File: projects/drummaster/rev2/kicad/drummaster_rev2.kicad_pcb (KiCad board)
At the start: 2 copper layers, 99.7 x 99.7 mm, 183 parts, among them K1 PINS_5, K1 PINS_7, K1 TSSOP-28, K2 DIP, K2 PINS_5, K2 PINS_7, K3 DIP, K3 MSSOP_10, K3 PINS_5, K4 PINS_4, K4 TSSOP_14, K5 PINS_6, K6 PINS_4, K7 ENCODER, P1 CONN_2, Q1 MOSFET_P, SW1 PROG, U1 TEENSY_3.1, U10 MCP46X1, U11 MCP46X1, U12 MCP46X1, U13 MCP46X1, U14 MCP46X1, U15 MCP46X1, U16 S25FL512S, U2 MCP6004T, U3 MCP6004T, U4 MCP6004T, U5 MCP6004T, U6 MCP6004T, U7 MCP6004T, U8 74HC4067, U9 74HC4067

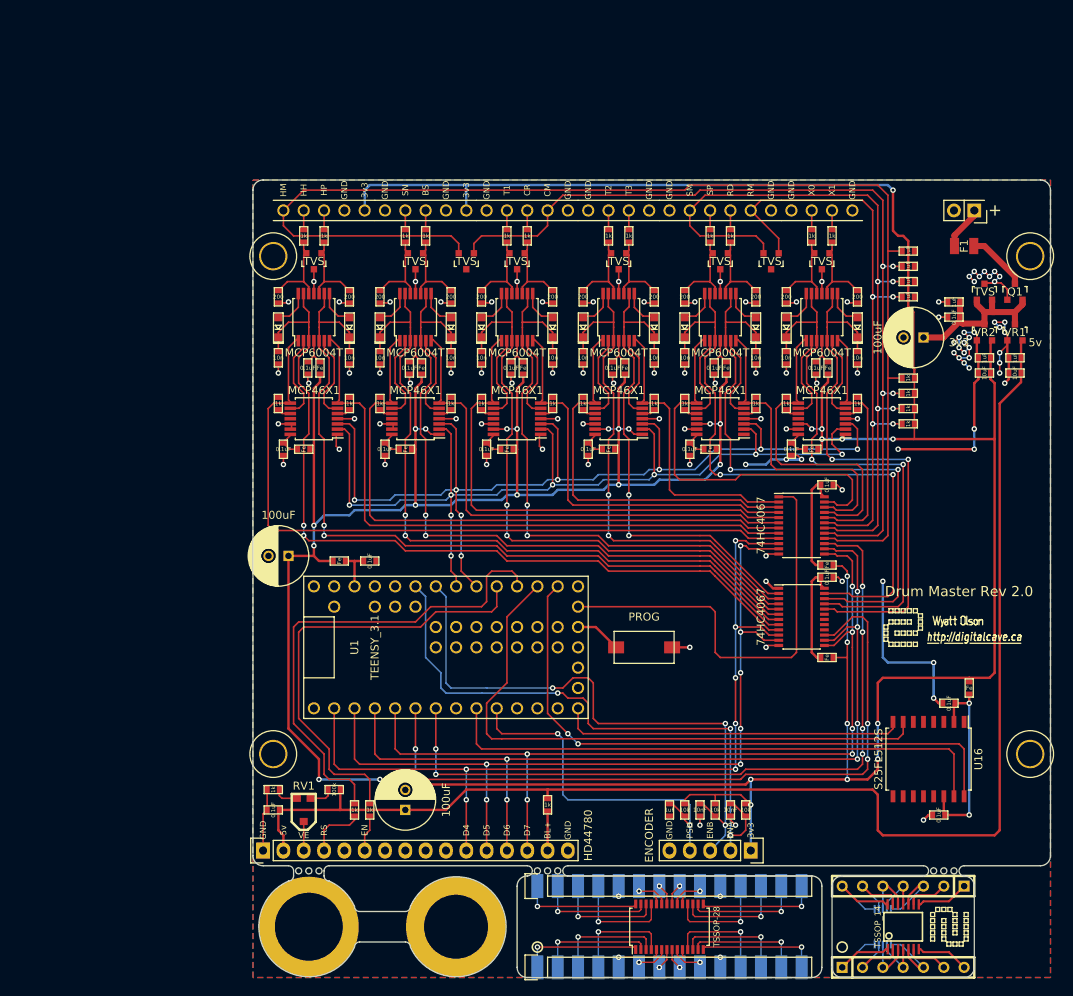
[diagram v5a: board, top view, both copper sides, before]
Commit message: Updated PCB page size
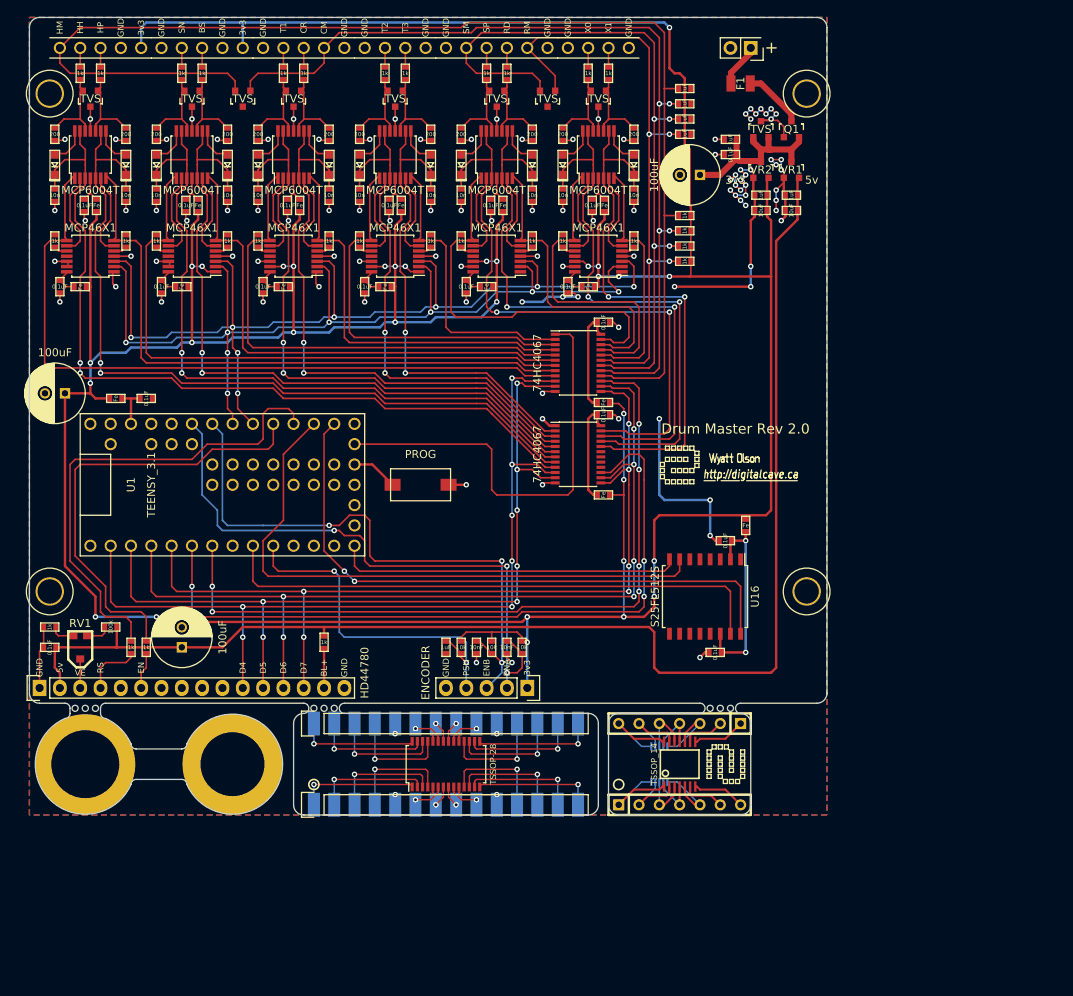
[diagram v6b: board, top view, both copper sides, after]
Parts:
- moved D20 34.5 mm to (94.6, 43.8)
- moved MP5 34.5 mm to (116.2, 80.6)
- moved MP7 34.5 mm to (118.1, 82.5)
- moved SW1 34.5 mm to (76.8, 83.8)
- moved mouse_bites 34.5 mm to (114.3, 111.8)
- moved C2 34.5 mm to (47.5, 48.9)
- moved C22 34.5 mm to (57.1, 59.1)
- moved C3 34.5 mm to (60.2, 48.9)
- moved C31 34.5 mm to (69.8, 59.1)
- moved D10 34.5 mm to (31.1, 43.8)
- moved D2 34.5 mm to (48.3, 35.6)
- moved D3 34.5 mm to (61.0, 35.6)
- moved D8 34.5 mm to (92.7, 35.6)
- moved K5 34.5 mm to (92.7, 29.2)
- moved L2 34.5 mm to (49.0, 48.9)
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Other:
- outline, holes or cut-outs redrawn
- net class Default: via_dia 0.889 -> 0.6858; via_drill 0.635 -> 0.3556
- rule via_min_drill: 0.508 -> 0.3556
- rule via_min_size: 0.889 -> 0.6858

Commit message: Tweaking layers on appended boards
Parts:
- K2, K3: moved to B.Cu
- turned K2 to 270 degrees
- turned K3 to 270 degrees

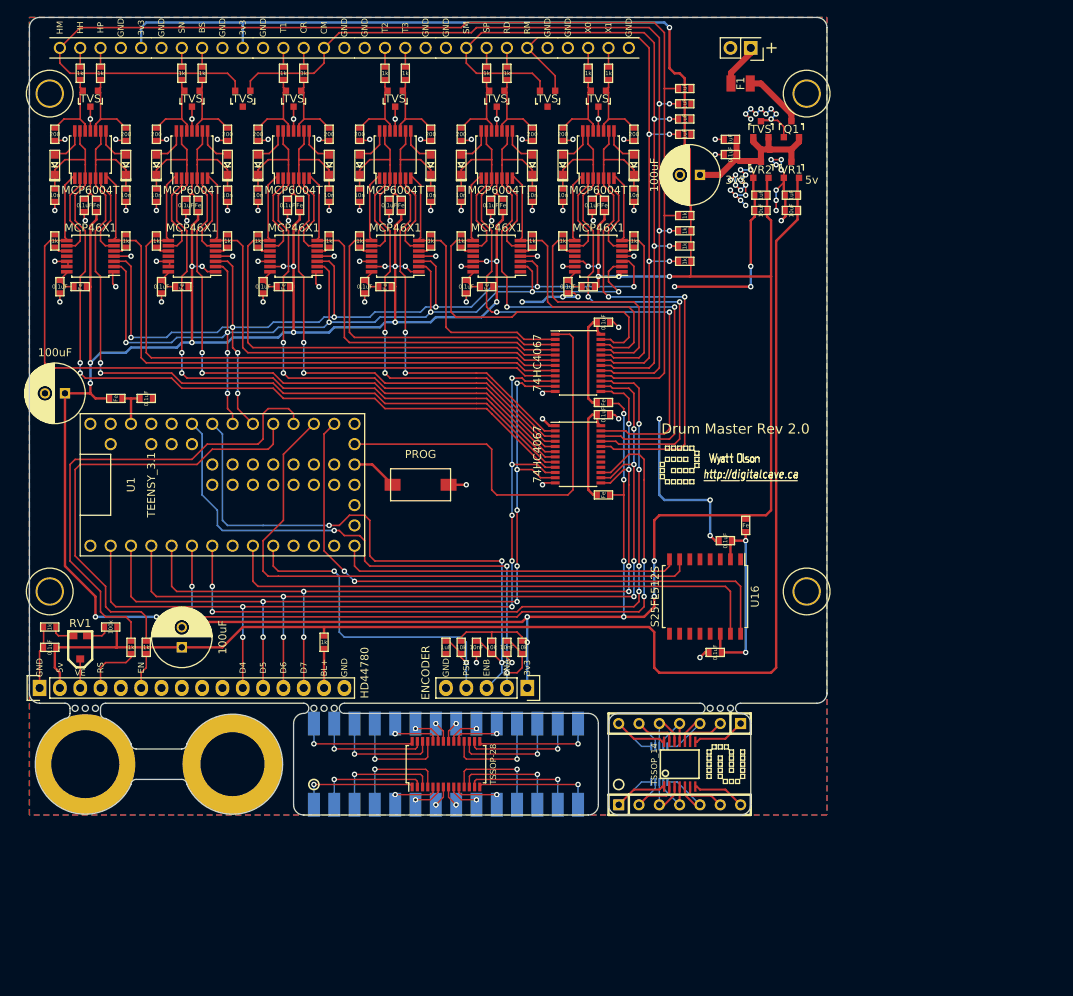
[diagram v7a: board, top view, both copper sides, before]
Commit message: Fixed some last minute bugs on drum master board, and added a TVS diode across 3.3v / 5v rails.
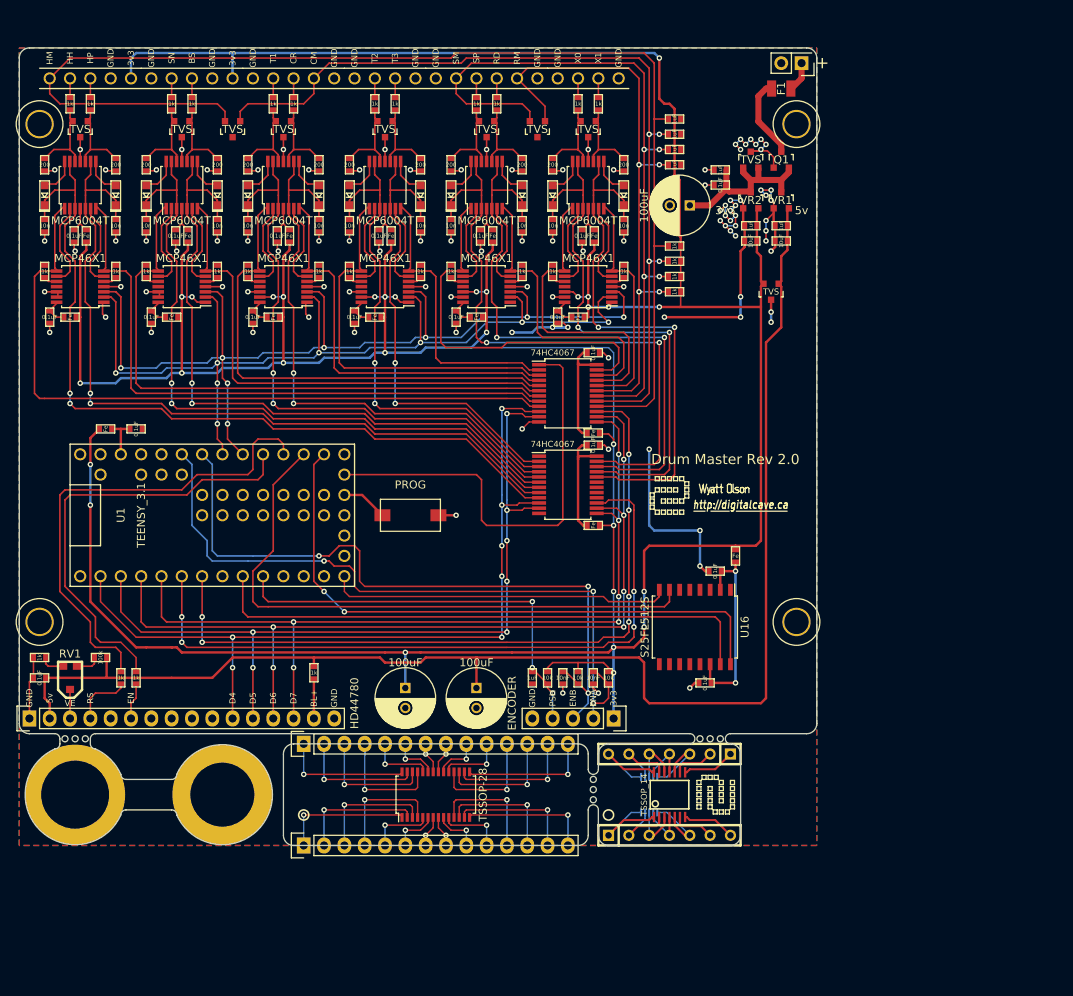
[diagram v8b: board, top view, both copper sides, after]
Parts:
- added D22: TVS, Housings_SOT-23_SOT-143_TSOT-6:SOT-23, F.Cu at (120.7, 59.7)
- K102: renamed from K2; moved to F.Cu
- K103: renamed from K3; moved to F.Cu
- U8, U9: footprint Housings_SSOP:TSSOP-24_4.4x7.8mm_Pitch0.65mm -> Housings_SSOP:SSOP-24_5.3x8.2mm_Pitch0.65mm
- moved C39 56.3 mm to (74.9, 109.2), turned to 270 degrees
- moved C24 37.2 mm to (83.8, 109.2), turned to 270 degrees
- moved mouse_bites 35.2 mm to (98.4, 121.9), turned to 90 degrees
- moved C40 11.4 mm to (98.4, 108.0)
- moved C41 11.4 mm to (94.6, 108.0)
- moved C42 11.4 mm to (90.8, 108.0)
- moved K7 11.4 mm to (101.0, 113.0)
- moved R22 11.4 mm to (100.3, 108.0)
- moved R23 11.4 mm to (96.5, 108.0)
- moved R24 11.4 mm to (92.7, 108.0)
- moved P1 6.63 mm to (124.5, 31.1)
- moved K102 5.24 mm to (62.2, 128.9), turned to 90 degrees
- moved F1 5.12 mm to (121.9, 34.3), turned to 180 degrees
- moved C13 4.02 mm to (76.8, 51.4)
- moved C14 4.02 mm to (67.9, 51.4)
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- renumbered K1 to K101, K1 to K201, K2 to K202, K3 to K203, K4 to K204
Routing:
- net +3V3: track 517.0 -> 534.0 mm, vias 31 -> 30
- net /ENC_B: track 74.2 -> 86.3 mm
- net /ENC_A: track 75.5 -> 87.6 mm
- net /ENC_PUSH: track 44.4 -> 52.3 mm, vias 2 -> 3
- net +5V: track 167.8 -> 172.4 mm
- net /MUX0: track 107.6 -> 103.5 mm
- net Net-(K1-Pad25): track 13.4 -> 17.2 mm
- net /DRAIN_ENABLE: track 90.6 -> 87.1 mm
- net Net-(K1-Pad11): track 13.4 -> 16.7 mm
- net /MUX1: track 103.2 -> 100.2 mm
- net Net-(F1-Pad2): track 7.63 -> 10.2 mm
- net /MUX3: track 106.8 -> 104.9 mm
- net /MUX2: track 112.6 -> 110.6 mm
- net +9V: track 5.47 -> 3.77 mm
- net /SP_A: track 49.7 -> 48.3 mm
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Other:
- outline, holes or cut-outs redrawn
